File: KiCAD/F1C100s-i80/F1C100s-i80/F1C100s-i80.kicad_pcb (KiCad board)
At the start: 2 copper layers, 48.3 x 78.7 mm, 88 parts, among them J1 LCD_I8080_CONNECTOR_16x2-DIP, J10 USB_B_Micro, J2 Key Export, J3 SPK, J4 LRADC, J5 UART, J7 Power, J8 Micro_SD_Card, J9 USB_A, M3 M3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

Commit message: c100s
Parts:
- moved J4 0.35 mm to (43.5, 34.3)
- moved R17 0.31 mm to (81.2, 87.5)
- moved J3 0.16 mm to (43.5, 42.8)
- moved R20 0.08 mm to (77.8, 87.5)
- renumbered TP1 to +1V2, TP2 to +2V5, TP3 to +3V3, SW1 to RST
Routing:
- net /DB15: track 20.1 -> 73.5 mm
- net GND: track 67.6 -> 79.3 mm, vias 13 -> 57
- net +2V5: track 59.1 -> 60.7 mm
- net Net-(C27-Pad2): track 9.26 -> 10.6 mm
- net /DB14: track 48.7 -> 49.6 mm
- net /DB13: track 49.8 -> 50.4 mm
- added copper zone on B.Cu, net GND
- added copper zone on F.Cu, net GND
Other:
- board text added: "+5V"
- board text added: ".T.R.E.S.S.A."
- board text added: "2019-12-28"
- board text added: "GND"
- board text added: "JLCJLCJLC"
- board text added: "KEY0"
- board text added: "KEY1"
- board text added: "KEY2"
- board text added: "KEY3"
- board text added: "KEY4"
- board text added: "KEY5"
- board text added: "KEY6"
- board text added: "LRADC"
- board text added: "RX"
- board text added: "SPK+"
- board text added: "SPK-"
- board text added: "TX"

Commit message: c100s&f40x
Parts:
- removed +1V2: +1V2, TestPoint:TestPoint_Pad_1.0x1.0mm
- added +1V1: +1V2, TestPoint:TestPoint_Pad_1.0x1.0mm, F.Cu at (79.2, 69.2)
- BT1: footprint Battery:BatteryHolder_Keystone_3000_1x12mm -> qmechanics:CR1220-2
- J9: footprint qconnectors:USB-AF -> qconnectors:USB-AF90
- R25, R26, R28, R29: value 0R -> 22R
- moved +2V5 9.25 mm to (83.3, 89.5)
- moved R17 6.50 mm to (74.7, 87.3), turned to 270 degrees
- moved R16 5.58 mm to (75.4, 72.0), turned to 90 degrees
- moved +3V3 4.85 mm to (68.0, 78.8)
- moved R21 4.60 mm to (72.1, 84.0), turned to 0 degrees
- moved C23 4.26 mm to (69.5, 83.3)
- moved C28 4.24 mm to (72.1, 82.4), turned to 0 degrees
- moved C26 4.11 mm to (76.1, 74.8)
- moved L3 3.91 mm to (80.6, 88.2), turned to 90 degrees
- moved J9 3.73 mm to (58.2, 32.7), turned to 0 degrees
- moved R18 2.98 mm to (72.1, 85.5), turned to 180 degrees
- moved L2 2.71 mm to (79.4, 72.6), turned to 270 degrees
- moved BT1 2.37 mm to (48.3, 55.9)
- moved C27 1.83 mm to (77.8, 87.3), turned to 90 degrees
- moved L4 1.68 mm to (71.5, 79.4), turned to 0 degrees
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- renumbered RST to SW1
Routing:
- net +5V: track 186.1 -> 234.0 mm, vias 6 -> 5
- net Net-(BT1-Pad1): track 67.6 -> 54.1 mm, vias 4 -> 3
- net +1V2: track 77.6 -> 90.4 mm
- net +3V3: track 168.6 -> 178.9 mm
- net Net-(C12-Pad1): track 20.2 -> 26.7 mm
- net GND: track 79.3 -> 85.6 mm, vias 57 -> 72
- net Net-(R31-Pad1): track 11.2 -> 16.1 mm
- net Net-(C26-Pad2): track 12.1 -> 7.51 mm
- net Net-(C27-Pad2): track 10.6 -> 7.85 mm
- net Net-(C28-Pad2): track 11.7 -> 9.38 mm
- net Net-(L3-Pad2): track 4.01 -> 6.20 mm
- net /KEY3: track 30.7 -> 32.7 mm
- net Net-(L4-Pad2): track 3.60 -> 5.01 mm
- net +2V5: track 60.7 -> 61.8 mm
- net /D-: track 14.1 -> 13.1 mm
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- added copper zone on F.Cu, net +1V2
- added copper zone on F.Cu, net +2V5
- added copper zone on F.Cu, net +3V3

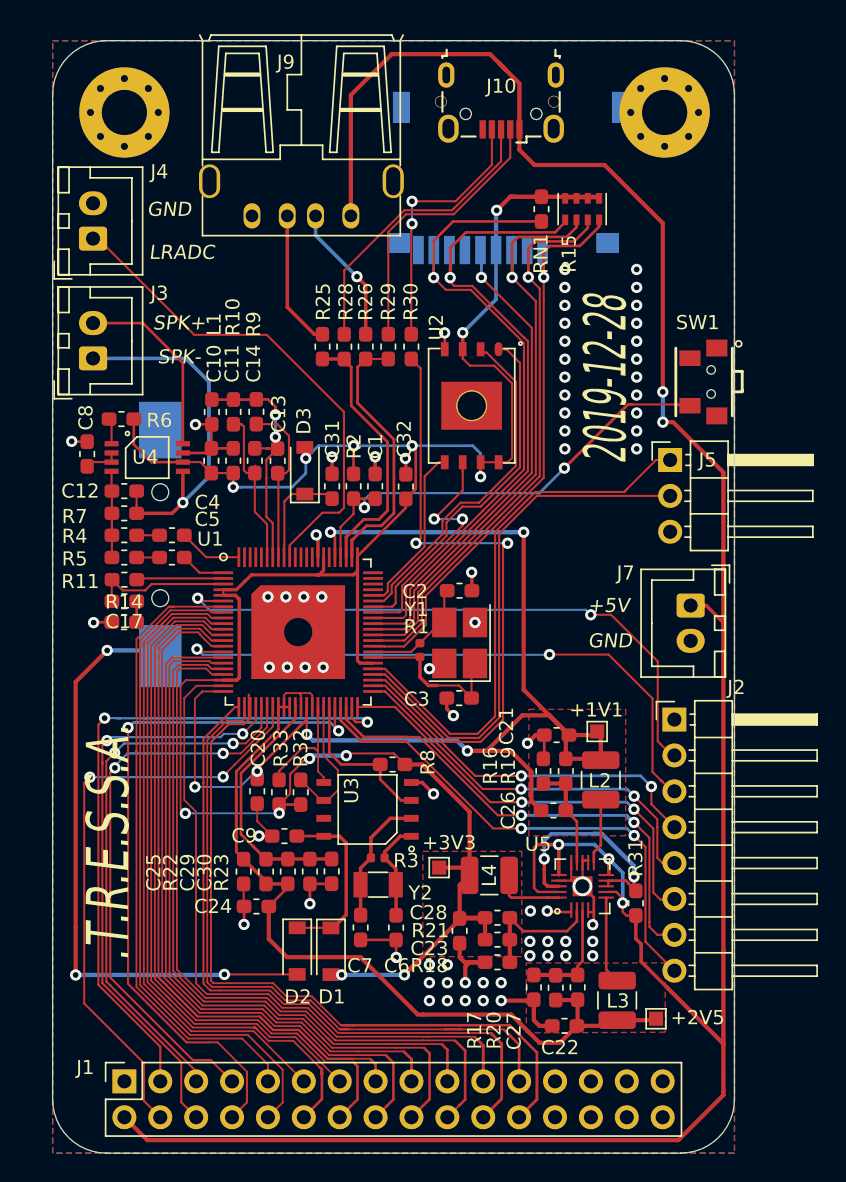
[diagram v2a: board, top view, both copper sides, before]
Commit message: 修改DCDC部分
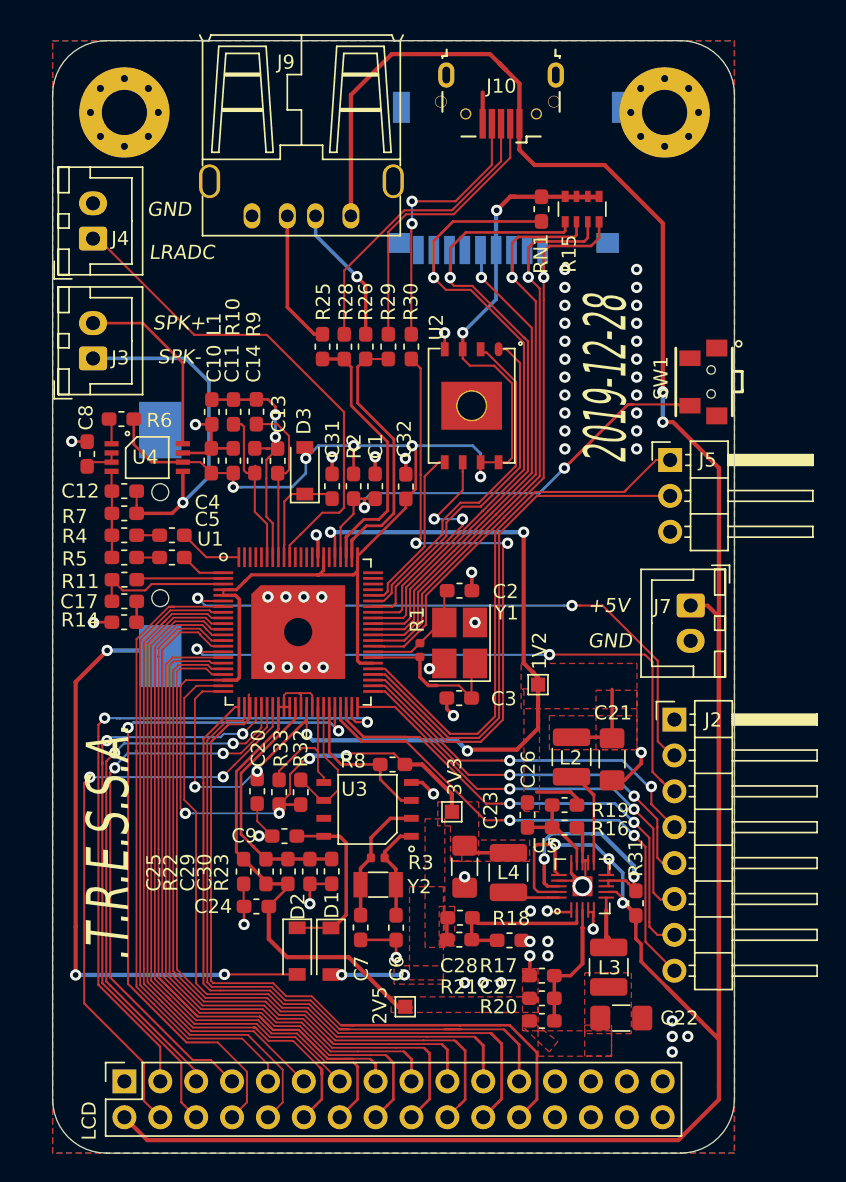
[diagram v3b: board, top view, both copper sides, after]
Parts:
- removed +2V5: +2V5, TestPoint:TestPoint_Pad_1.0x1.0mm
- added 2V5: +2V5, TestPoint:TestPoint_Pad_1.0x1.0mm, F.Cu at (65.6, 88.7)
- C21, C22, C23: footprint Capacitor_SMD:C_0603_1608Metric_Pad1.05x0.95mm_HandSolder -> Capacitor_SMD:C_1206_3216Metric_Pad1.42x1.75mm_HandSolder
- J10: footprint Connector_USB:USB_Micro-B_Wuerth_629105150521 -> qconnectors:USB_Micro
- RN1: footprint Resistor_SMD:R_Cat16-4 -> Resistor_SMD:R_Array_Convex_4x0603
- moved 1V2 5.34 mm to (75.0, 65.9)
- moved C23 4.55 mm to (69.8, 78.8)
- moved C21 4.28 mm to (80.2, 71.2), turned to 270 degrees
- moved R16 4.27 mm to (76.9, 76.0), turned to 0 degrees
- moved 3V3 4.05 mm to (68.9, 74.9)
- moved C22 4.05 mm to (80.9, 89.5), turned to 0 degrees
- moved R21 2.70 mm to (69.4, 84.0)
- moved C28 2.65 mm to (69.5, 82.4)
- moved C27 2.64 mm to (75.3, 88.1), turned to 0 degrees
- moved L2 2.63 mm to (77.4, 71.0)
- moved R20 2.54 mm to (75.3, 89.7), turned to 0 degrees
- moved L3 2.43 mm to (80.0, 85.9)
- moved R19 2.40 mm to (76.9, 74.4), turned to 180 degrees
- moved C26 1.87 mm to (74.2, 75.1), turned to 270 degrees
- moved R18 1.77 mm to (73.0, 84.0), turned to 0 degrees
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- renumbered +1V1 to 1V2, +3V3 to 3V3, J1 to LCD
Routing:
- net +2V5: track 61.8 -> 38.3 mm
- net +3V3: track 178.9 -> 160.8 mm
- net +5V: track 234.0 -> 216.4 mm
- net +1V2: track 90.4 -> 79.2 mm
- net GND: track 85.6 -> 80.7 mm, vias 72 -> 64
- net Net-(C28-Pad2): track 9.38 -> 12.0 mm
- net Net-(L2-Pad2): track 4.66 -> 7.10 mm
- net /KEY1: track 43.1 -> 44.6 mm
- net Net-(C27-Pad2): track 7.85 -> 9.35 mm
- net Net-(L4-Pad2): track 5.01 -> 3.58 mm
- net /KEY3: track 32.7 -> 31.5 mm
- net /KEY4: track 35.0 -> 34.1 mm
- net Net-(C26-Pad2): track 7.51 -> 6.72 mm

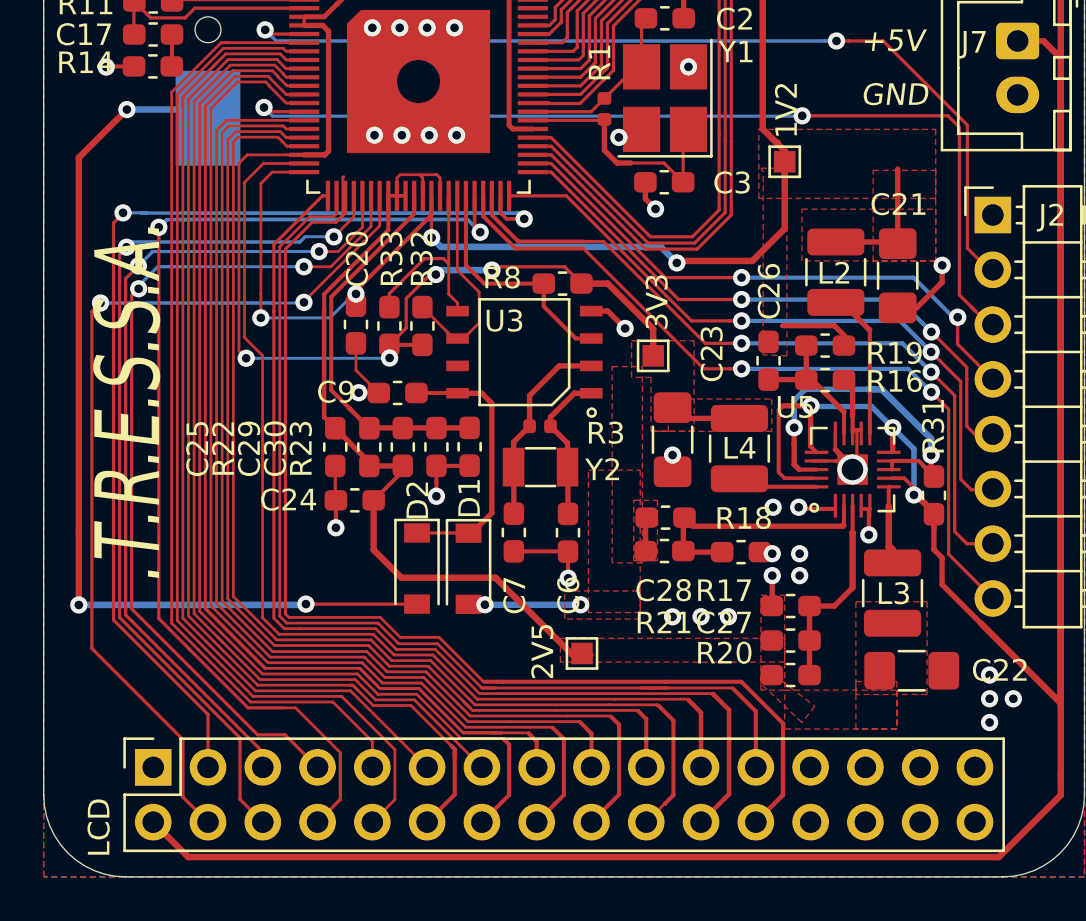
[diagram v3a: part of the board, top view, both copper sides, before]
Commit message: 更改C100s走线
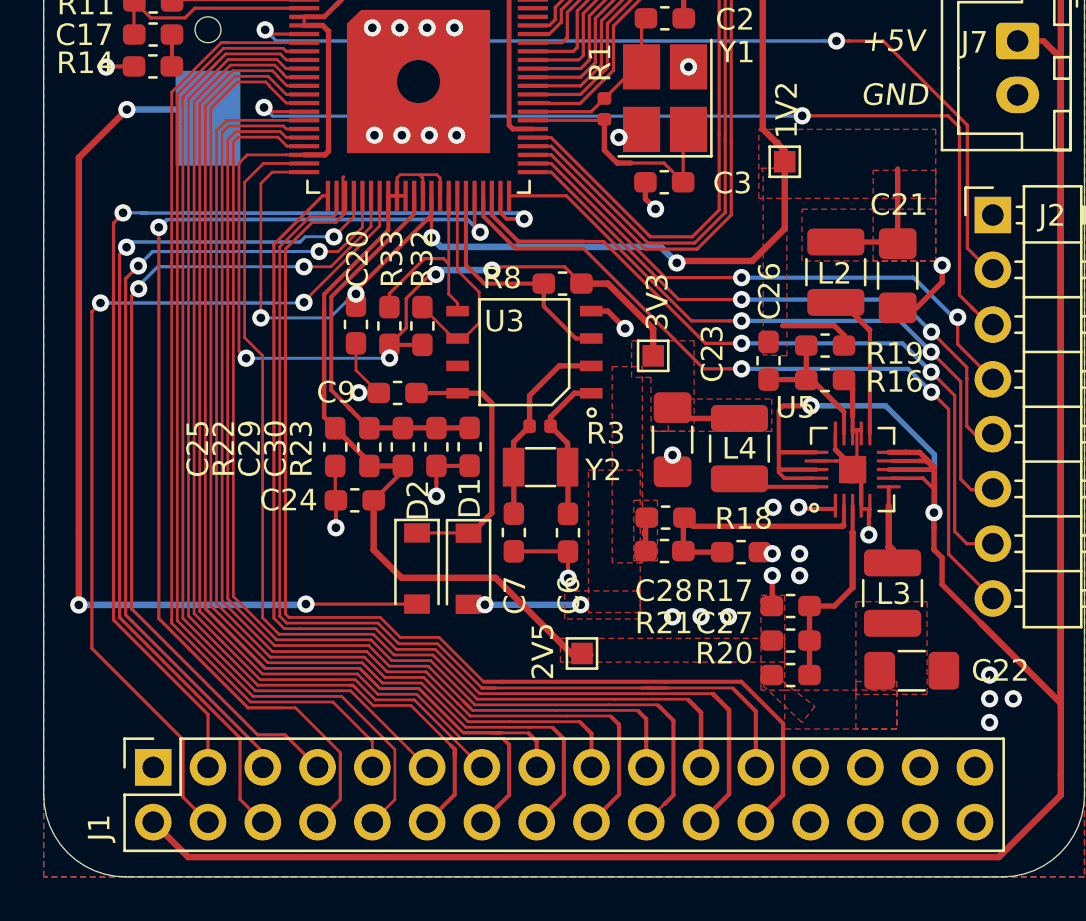
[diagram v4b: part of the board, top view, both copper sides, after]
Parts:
- removed R31: 1K, Resistor_SMD:R_0603_1608Metric_Pad1.05x0.95mm_HandSolder
- R17: value 47K -> 150K
- R20: value 152K -> 510K
- renumbered LCD to J1
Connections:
- U5 pad 18: Net-(R31-Pad1) -> +5V
- U5 pad 8: Net-(R31-Pad1) -> +5V
- U5 pad 9: Net-(R31-Pad1) -> +5V
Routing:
- net Net-(R31-Pad1): track 16.1 -> 0.00 mm, vias 2 -> 0
- net +5V: track 216.4 -> 227.5 mm, vias 5 -> 4
- net GND: track 80.7 -> 82.8 mm, vias 64 -> 63
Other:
- board text removed: ".T.R.E.S.S.A."

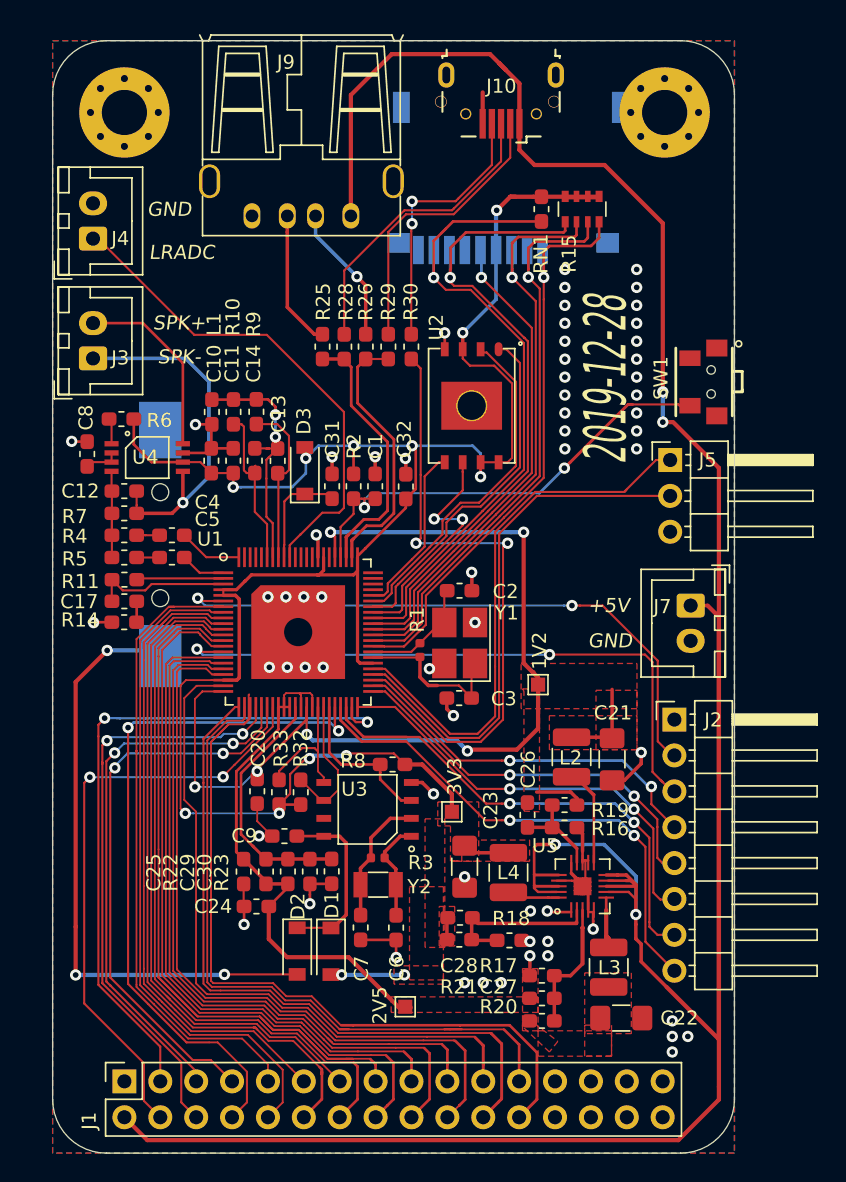
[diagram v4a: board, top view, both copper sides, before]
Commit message: 修改排阻为0603电阻
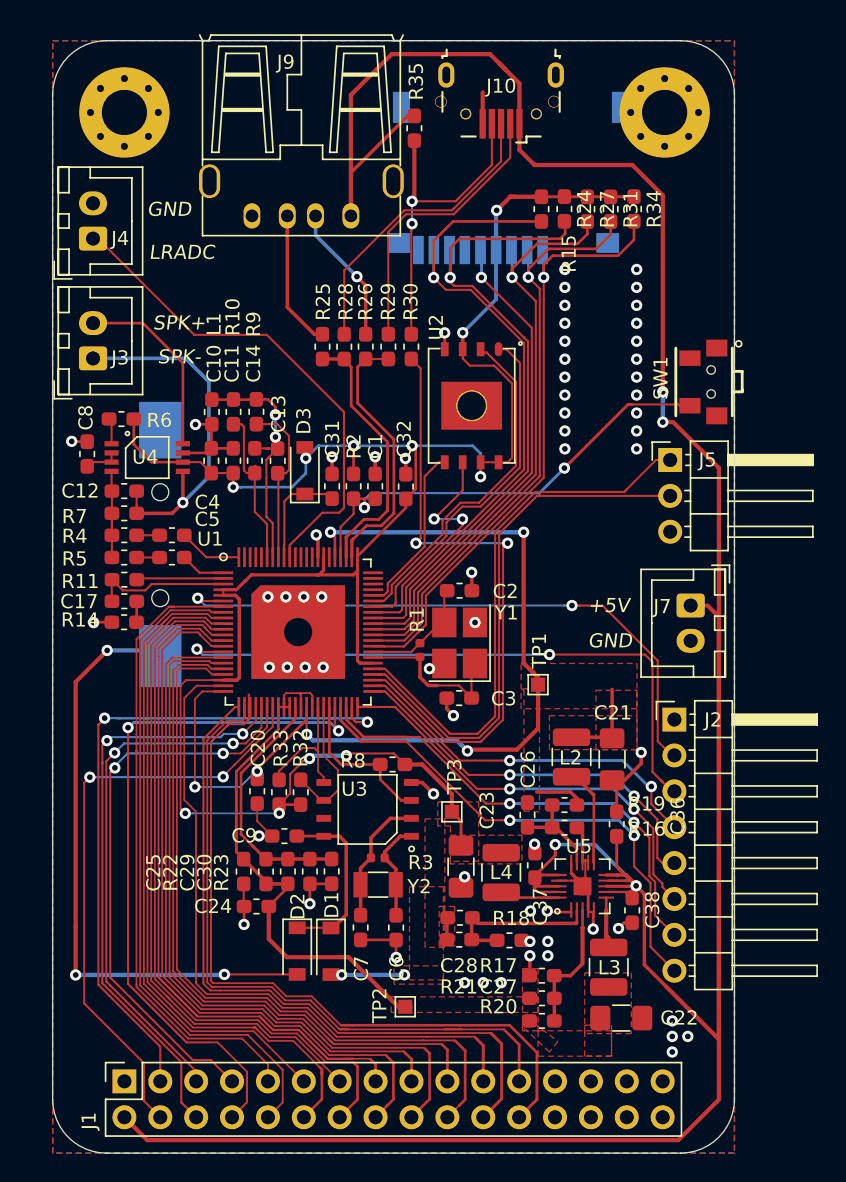
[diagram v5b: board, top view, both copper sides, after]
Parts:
- removed RN1: 47K, Resistor_SMD:R_Array_Convex_4x0603
- added C36: 100nF, Capacitor_SMD:C_0603_1608Metric_Pad1.05x0.95mm_HandSolder, F.Cu at (80.6, 75.8)
- added C37: 100nF, Capacitor_SMD:C_0603_1608Metric_Pad1.05x0.95mm_HandSolder, F.Cu at (74.8, 78.7)
- added C38: 100nF, Capacitor_SMD:C_0603_1608Metric_Pad1.05x0.95mm_HandSolder, F.Cu at (81.7, 81.9)
- added R24: 47K, Resistor_SMD:R_0603_1608Metric_Pad1.05x0.95mm_HandSolder, F.Cu at (76.9, 32.2)
- added R27: 47K, Resistor_SMD:R_0603_1608Metric_Pad1.05x0.95mm_HandSolder, F.Cu at (78.5, 32.2)
- added R31: 47K, Resistor_SMD:R_0603_1608Metric_Pad1.05x0.95mm_HandSolder, F.Cu at (80.1, 32.2)
- added R34: 47K, Resistor_SMD:R_0603_1608Metric_Pad1.05x0.95mm_HandSolder, F.Cu at (81.8, 32.2)
- added R35: 0R, Resistor_SMD:R_0603_1608Metric_Pad1.05x0.95mm_HandSolder, F.Cu at (66.2, 26.5)
- moved L4 0.51 mm to (72.4, 79.2)
- moved C23 0.25 mm to (69.5, 78.8)
- renumbered 1V2 to TP1, 2V5 to TP2, 3V3 to TP3
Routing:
- net +5V: track 227.5 -> 236.7 mm
- net Net-(J10-Pad4): track 18.2 -> 22.6 mm
- net GND: track 82.8 -> 86.9 mm, vias 63 -> 65
- net /SDC0_D2: track 41.5 -> 43.4 mm
- net +3V3: track 160.8 -> 159.1 mm
- net /KEY4: track 34.1 -> 33.4 mm
- net /KEY3: track 31.5 -> 30.8 mm
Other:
- board text removed: "2019-12-28"
